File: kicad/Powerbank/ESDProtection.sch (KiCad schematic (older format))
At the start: 1 part

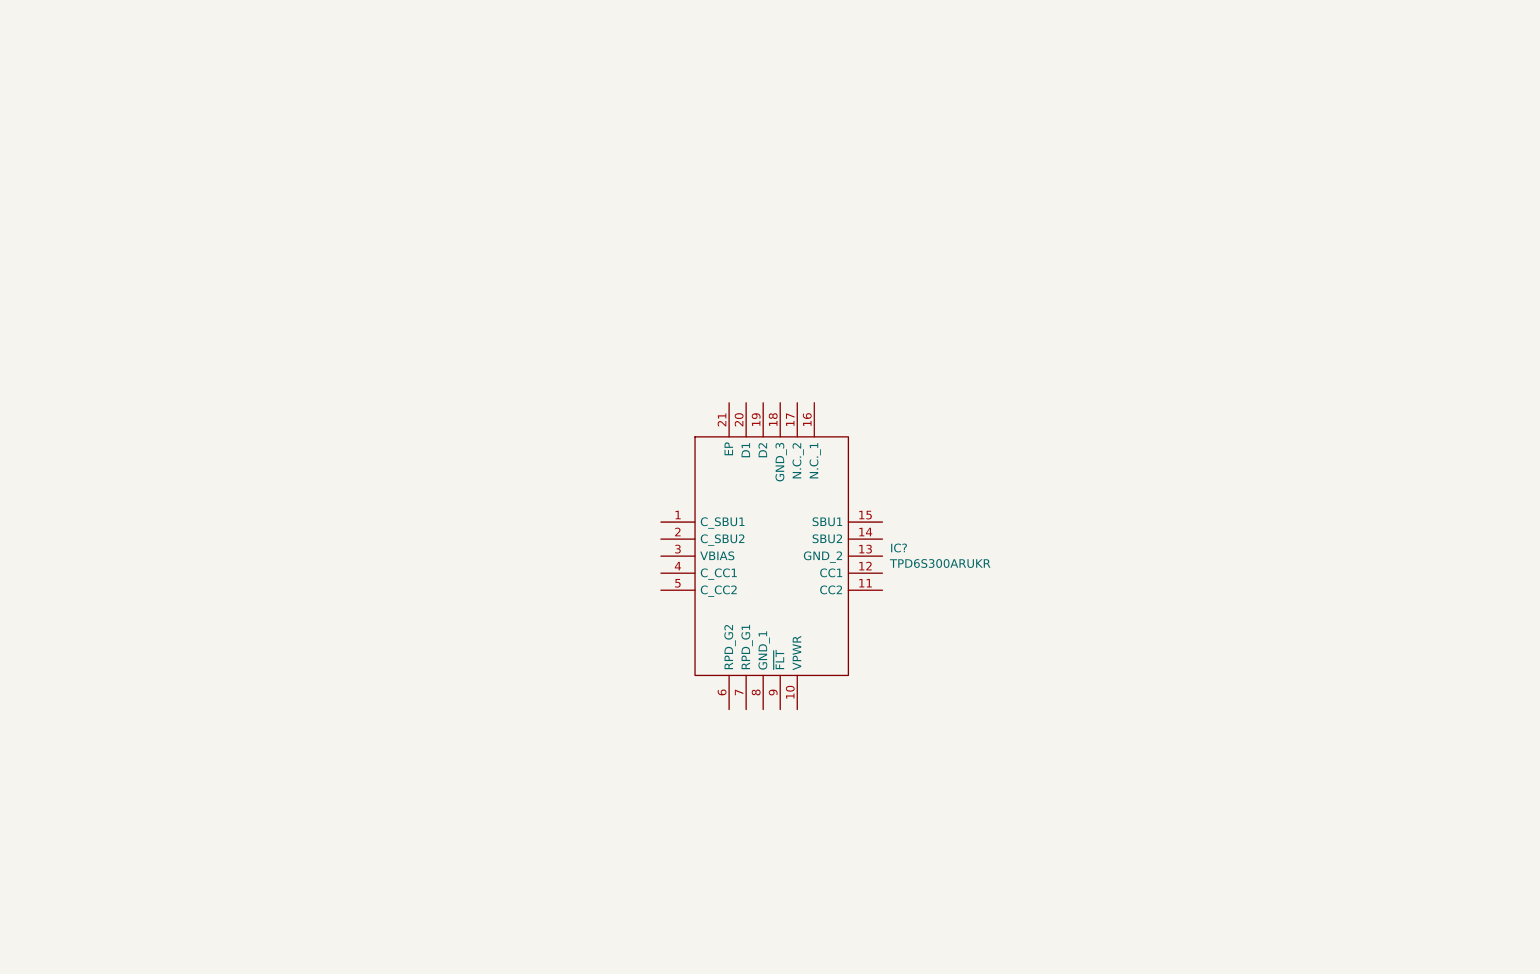
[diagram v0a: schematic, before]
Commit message: Added USB C + A and protection circuit according to ref. design
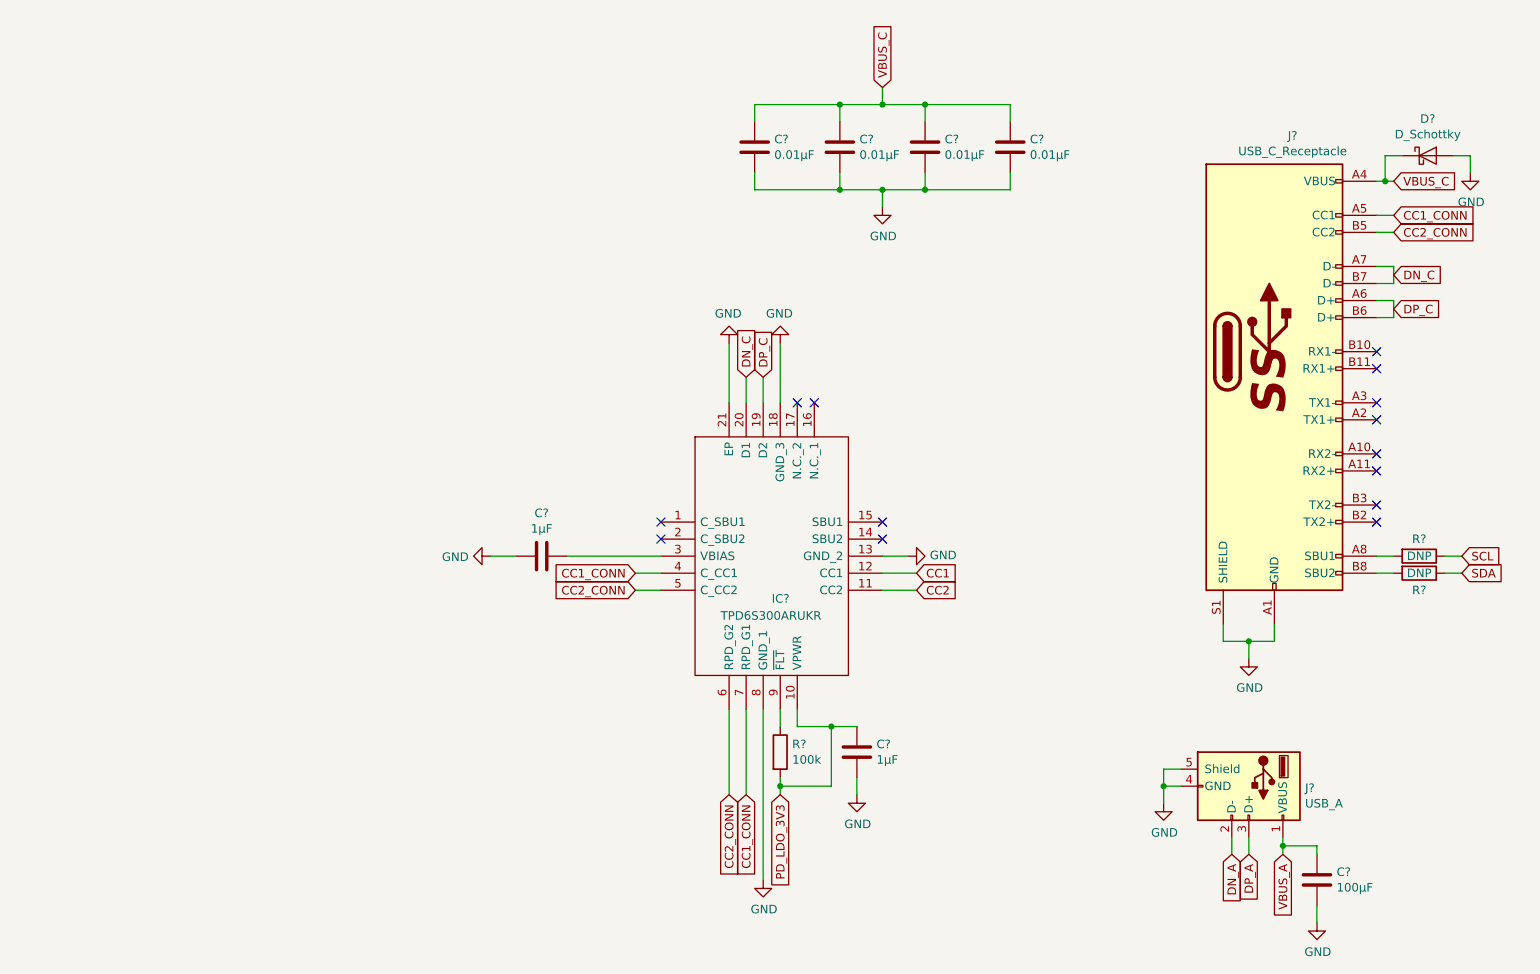
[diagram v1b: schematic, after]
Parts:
- added C? (x2): 1µF, symbol Device:C
- added C? (x4): 0.01µF, symbol Device:C
- added C?: 100µF, symbol Device:C
- added D?: D_Schottky, symbol Device:D_Schottky
- added J?: USB_C_Receptacle, symbol Connector:USB_C_Receptacle
- added J?: USB_A, symbol Connector:USB_A
- added R?: 100k, symbol Device:R
- added R? (x2): DNP, symbol Device:R
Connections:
- net PD_LDO_3V3: now reaches IC?.10 (VPWR)
- net PD_LDO_3V3: now also C?.2, R?.2
- net CC2: now reaches IC?.11 (CC2)
- net CC1: now reaches IC?.12 (CC1)
- net GND: now reaches IC?.13 (GND_2)
- net GND: now also IC?.18 (GND_3), IC?.21 (EP), IC?.8 (GND_1), C?.1, C?.1, C?.1, C?.1, C?.1, C?.1, C?.2, D?.2 (A), J?.4 (GND), J?.5 (Shield), J?.A1 (GND), J?.A12 (GND), J?.B1 (GND), J?.B12 (GND), J?.S1 (SHIELD)
- net DP_C: now reaches IC?.19 (D2)
- net DP_C: now also J?.A6 (D+), J?.B6 (D+)
- net DN_C: now reaches IC?.20 (D1)
- net DN_C: now also J?.A7 (D-), J?.B7 (D-)
- net at IC?.3 (VBIAS): now also C?.2
- net CC1_CONN: now reaches IC?.4 (C_CC1)
- net CC1_CONN: now also IC?.7 (RPD_G1), J?.A5 (CC1)
- net CC2_CONN: now reaches IC?.5 (C_CC2)
- net CC2_CONN: now also IC?.6 (RPD_G2), J?.B5 (CC2)
- net at IC?.9 (~FLT): now also R?.1
- new net: J?.A8 (SBU1), R?.2
- new net: J?.B8 (SBU2), R?.2
- new net DN_A: J?.2 (D-)
- new net DP_A: J?.3 (D+)
- new net SCL: R?.1
- new net SDA: R?.1
- new net VBUS_A: C?.1, J?.1 (VBUS)
- new net VBUS_C: C?.2, C?.2, C?.2, C?.2, D?.1 (K), J?.A4 (VBUS), J?.A9 (VBUS), J?.B4 (VBUS), J?.B9 (VBUS)
- no-connect marks 0 -> 14

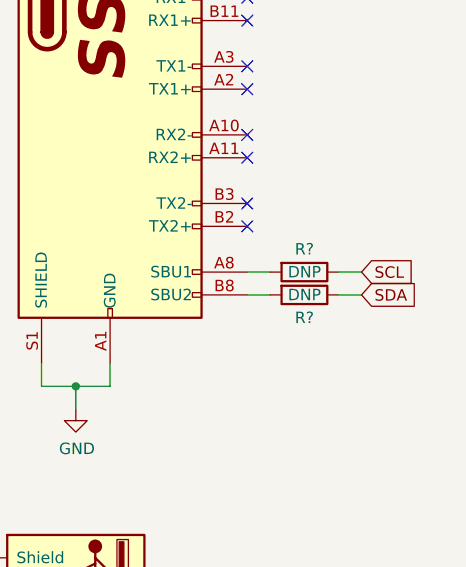
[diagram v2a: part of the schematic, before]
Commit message: Moved LDO to Buck sheet and started check of components
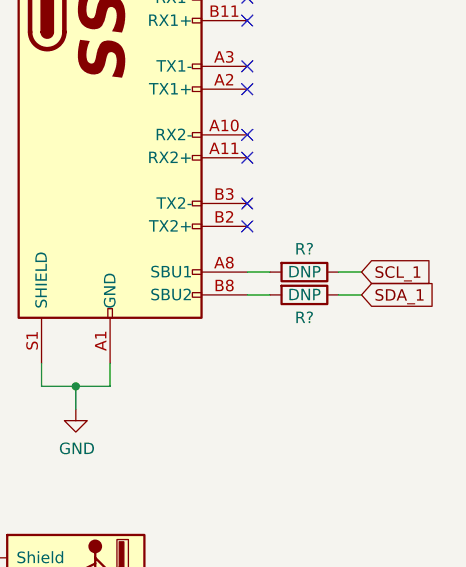
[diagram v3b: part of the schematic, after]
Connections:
- net SCL renamed SCL_1
- net SDA renamed SDA_1
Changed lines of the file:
@@
 $Descr A4 11693 8268
 encoding utf-8
-Sheet 4 8
+Sheet 4 7
 Title ""
 Date ""
@@
 $EndComp
 Text GLabel 9800 3700 2    50   Input ~ 0
-SCL
+SCL_1
 Text GLabel 9800 3800 2    50   Input ~ 0
-SDA
+SDA_1
 Wire Wire Line
 	9300 3700 9400 3700

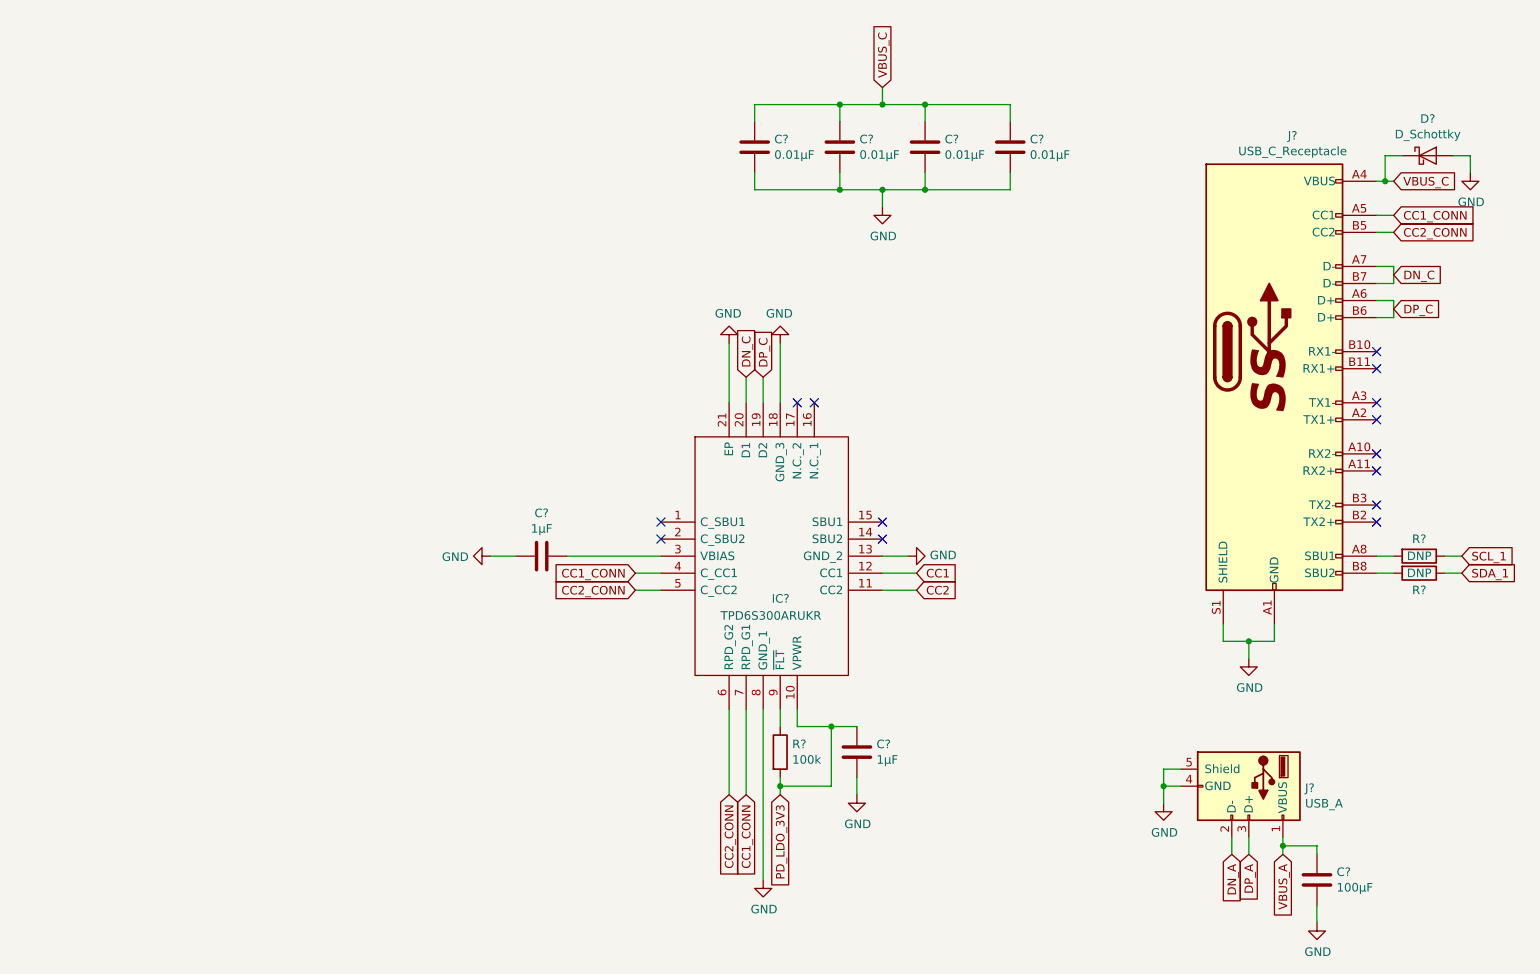
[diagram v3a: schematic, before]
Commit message: Double checked schematic towards reference design
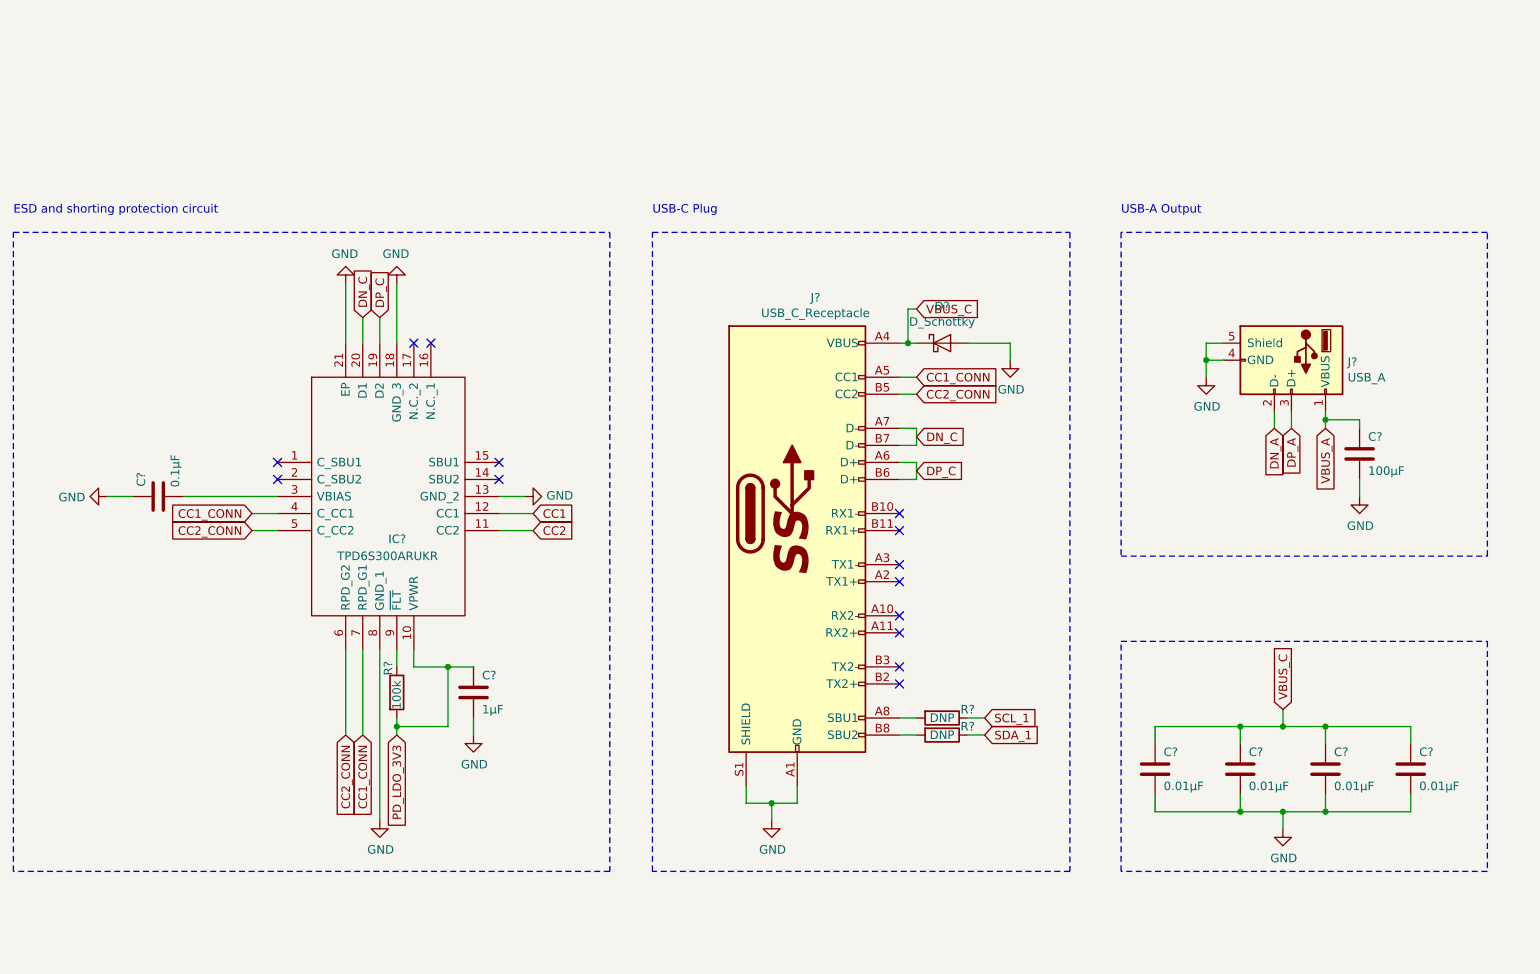
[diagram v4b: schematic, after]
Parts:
- C?: value 1µF -> 0.1µF
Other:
- note added: "ESD and shorting protection circuit"
- note added: "USB-A Output"
- note added: "USB-C Plug"
- moved on the sheet: C?, D?, IC?, J?, R?

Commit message: Update ESDProtection.sch
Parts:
- C35, C36, C37, C38, C39, C41: renamed from C?; footprint (none) -> Capacitor_SMD:C_0603_1608Metric
- IC5: renamed from IC?; footprint QFN40P300X300X80-21N-D -> Powerbank:QFN40P300X300X80-21N-D
- J1: renamed from J?; footprint (none) -> Connector_USB:USB_C_Receptacle_Amphenol_12401610E4-2A
- J2: renamed from J?; footprint (none) -> Connector_USB:USB_A_Stewart_SS-52100-001_Horizontal
- R49, R50, R51: renamed from R?; footprint (none) -> Resistor_SMD:R_0603_1608Metric
- gave numbers to parts that had none: 2
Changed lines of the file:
@@
 EESchema Schematic File Version 4
+LIBS:Powerbank-cache
 EELAYER 30 0
 EELAYER END
@@
 PD_LDO_3V3
 $Comp
-L Device:R R?
+L Device:R R49
 U 1 1 5E747B88
 P 3550 4500
-F 0 "R?" V 3500 4600 50  0000 L CNN
+F 0 "R49" V 3500 4600 50  0000 L CNN
 F 1 "100k" V 3550 4400 50  0000 L CNN
-F 2 "" V 3480 4500 50  0001 C CNN
+F 2 "Resistor_SMD:R_0603_1608Metric" V 3480 4500 50  0001 C CNN
 F 3 "~" H 3550 4500 50  0001 C CNN
 	1    3550 4500
@@
 	3450 4250 3450 5250
 $Comp
-L Device:C C?
+L Device:C C36
 U 1 1 5E74EE70
 P 4000 4500
-F 0 "C?" H 3950 4400 50  0000 R CNN
+F 0 "C36" H 3950 4400 50  0000 R CNN
 F 1 "1µF" H 3950 4600 50  0000 R CNN
-F 2 "" H 4038 4350 50  0001 C CNN
+F 2 "Capacitor_SMD:C_0603_1608Metric" H 4038 4350 50  0001 C CNN
 F 3 "~" H 4000 4500 50  0001 C CNN
 	1    4000 4500
@@
 	4000 4750 4000 4650
 $Comp
-L Device:C C?
+L Device:C C35
 U 1 1 5E752C26
 P 2150 3350
-F 0 "C?" H 2250 3450 50  0000 C CNN
+F 0 "C35" H 2250 3450 50  0000 C CNN
 F 1 "0.1µF" H 2300 3250 50  0000 C CNN
-F 2 "" H 2188 3200 50  0001 C CNN
+F 2 "Capacitor_SMD:C_0603_1608Metric" H 2188 3200 50  0001 C CNN
 F 3 "~" H 2150 3350 50  0001 C CNN
 	1    2150 3350
@@
 CC2_CONN
 $Comp
-L Powerbank:TPD6S300ARUKR IC?
+L Powerbank:TPD6S300ARUKR IC5
 U 1 1 5E0D0685
 P 2850 3150
-F 0 "IC?" H 3500 2700 50  0000 L CNN
+F 0 "IC5" H 3500 2700 50  0000 L CNN
 F 1 "TPD6S300ARUKR" H 3200 2600 50  0000 L CNN
-F 2 "QFN40P300X300X80-21N-D" H 4000 3650 50  0001 L CNN
+F 2 "Powerbank:QFN40P300X300X80-21N-D" H 4000 3650 50  0001 L CNN
 F 3 "http://www.ti.com/lit/gpn/tpd6s300a" H 4000 3550 50  0001 L CNN
 F 4 "USB Type-C Port Protector Short-to-VBUS Overvoltage and IEC ESD Protection" H 4000 3450 50  0001 L CNN "Description"
@@
 NoConn ~ 4150 3250
 $Comp
-L Device:C C?
+L Device:C C41
 U 1 1 5E7648D0
 P 9500 4950
-F 0 "C?" H 9450 4850 50  0000 R CNN
+F 0 "C41" H 9450 4850 50  0000 R CNN
 F 1 "0.01µF" H 9450 5050 50  0000 R CNN
-F 2 "" H 9538 4800 50  0001 C CNN
+F 2 "Capacitor_SMD:C_0603_1608Metric" H 9538 4800 50  0001 C CNN
 F 3 "~" H 9500 4950 50  0001 C CNN
 	1    9500 4950
@@
 $EndComp
 $Comp
-L Device:C C?
+L Device:C C39
 U 1 1 5E7654CB
 P 9000 4950
-F 0 "C?" H 8950 4850 50  0000 R CNN
+F 0 "C39" H 8950 4850 50  0000 R CNN
 F 1 "0.01µF" H 8950 5050 50  0000 R CNN
-F 2 "" H 9038 4800 50  0001 C CNN
+F 2 "Capacitor_SMD:C_0603_1608Metric" H 9038 4800 50  0001 C CNN
 F 3 "~" H 9000 4950 50  0001 C CNN
 	1    9000 4950
@@
 $EndComp
 $Comp
-L Device:C C?
+L Device:C C38
 U 1 1 5E76584E
 P 8500 4950
-F 0 "C?" H 8450 4850 50  0000 R CNN
+F 0 "C38" H 8450 4850 50  0000 R CNN
 F 1 "0.01µF" H 8450 5050 50  0000 R CNN
-F 2 "" H 8538 4800 50  0001 C CNN
+F 2 "Capacitor_SMD:C_0603_1608Metric" H 8538 4800 50  0001 C CNN
 F 3 "~" H 8500 4950 50  0001 C CNN
 	1    8500 4950
@@
 $EndComp
 $Comp
-L Device:C C?
+L Device:C C37
 U 1 1 5E765BA5
 P 8000 4950
-F 0 "C?" H 7950 4850 50  0000 R CNN
+F 0 "C37" H 7950 4850 50  0000 R CNN
 F 1 "0.01µF" H 7950 5050 50  0000 R CNN
-F 2 "" H 8038 4800 50  0001 C CNN
+F 2 "Capacitor_SMD:C_0603_1608Metric" H 8038 4800 50  0001 C CNN
 F 3 "~" H 8000 4950 50  0001 C CNN
 	1    8000 4950
@@
 	8750 5200 9000 5200
 $Comp
-L Connector:USB_C_Receptacle J?
+L Connector:USB_C_Receptacle J1
 U 1 1 5E7701C7
 P 5900 3450
-F 0 "J?" H 6007 4717 50  0000 C CNN
+F 0 "J1" H 6007 4717 50  0000 C CNN
 F 1 "USB_C_Receptacle" H 6007 4626 50  0000 C CNN
-F 2 "" H 6050 3450 50  0001 C CNN
+F 2 "Connector_USB:USB_C_Receptacle_Amphenol_12401610E4-2A" H 6050 3450 50  0001 C CNN
 F 3 "https://www.usb.org/sites/default/files/documents/usb_type-c.zip" H 6050 3450 50  0001 C CNN
 	1    5900 3450
@@
 	6500 4650 6600 4650
 $Comp
-L Device:R R?
+L Device:R R50
 U 1 1 5E796567
 P 6750 4650
-F 0 "R?" V 6700 4800 50  0000 C CNN
+F 0 "R50" V 6700 4800 50  0000 C CNN
 F 1 "DNP" V 6750 4650 50  0000 C CNN
-F 2 "" V 6680 4650 50  0001 C CNN
+F 2 "Resistor_SMD:R_0603_1608Metric" V 6680 4650 50  0001 C CNN
 F 3 "~" H 6750 4650 50  0001 C CNN
 	1    6750 4650
@@
 	6600 4750 6500 4750
 $Comp
-L Device:R R?
+L Device:R R51
 U 1 1 5E795208
 P 6750 4750
-F 0 "R?" V 6700 4900 50  0000 C CNN
+F 0 "R51" V 6700 4900 50  0000 C CNN
 F 1 "DNP" V 6750 4750 50  0000 C CNN
-F 2 "" V 6680 4750 50  0001 C CNN
+F 2 "Resistor_SMD:R_0603_1608Metric" V 6680 4750 50  0001 C CNN
 F 3 "~" H 6750 4750 50  0001 C CNN
 	1    6750 4750
@@
 	6900 4750 7000 4750
 $Comp
-L Connector:USB_A J?
+L Connector:USB_A J2
 U 1 1 5E7A4D3B
 P 8800 2550
-F 0 "J?" V 8811 2880 50  0000 L CNN
+F 0 "J2" V 8811 2880 50  0000 L CNN
 F 1 "USB_A" V 8902 2880 50  0000 L CNN
-F 2 "" H 8950 2500 50  0001 C CNN
+F 2 "Connector_USB:USB_A_Stewart_SS-52100-001_Horizontal" H 8950 2500 50  0001 C CNN
 F 3 " ~" H 8950 2500 50  0001 C CNN
 	1    8800 2550
@@
 	8300 2550 8300 2450
 $Comp
-L Device:C C?
+L Device:C C40
 U 1 1 5E7AEAC1
 P 9200 3100
-F 0 "C?" H 9250 3200 50  0000 L CNN
+F 0 "C40" H 9250 3200 50  0000 L CNN
 F 1 "100µF" H 9250 3000 50  0000 L CNN
 F 2 "" H 9238 2950 50  0001 C CNN
@@
 	6500 2450 6550 2450
 $Comp
-L Device:D_Schottky D?
+L Device:D_Schottky D7
 U 1 1 5E78B23C
 P 6750 2450
-F 0 "D?" H 6750 2666 50  0000 C CNN
+F 0 "D7" H 6750 2666 50  0000 C CNN
 F 1 "D_Schottky" H 6750 2575 50  0000 C CNN
 F 2 "" H 6750 2450 50  0001 C CNN

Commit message: Added footprint for all, moved to a first attempt for routing
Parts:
- D7: footprint (none) -> Diode_SMD:D_0603_1608Metric
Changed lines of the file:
@@
 F 0 "D7" H 6750 2666 50  0000 C CNN
 F 1 "D_Schottky" H 6750 2575 50  0000 C CNN
-F 2 "" H 6750 2450 50  0001 C CNN
+F 2 "Diode_SMD:D_0603_1608Metric" H 6750 2450 50  0001 C CNN
 F 3 "~" H 6750 2450 50  0001 C CNN
 	1    6750 2450

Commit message: DRC almost finished and added cap for USB-A
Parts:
- C40: footprint (none) -> Capacitor_Tantalum_SMD:CP_EIA-7343-15_Kemet-W
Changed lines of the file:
@@
 F 0 "C40" H 9250 3200 50  0000 L CNN
 F 1 "100µF" H 9250 3000 50  0000 L CNN
-F 2 "" H 9238 2950 50  0001 C CNN
+F 2 "Capacitor_Tantalum_SMD:CP_EIA-7343-15_Kemet-W" H 9238 2950 50  0001 C CNN
 F 3 "~" H 9200 3100 50  0001 C CNN
 	1    9200 3100
